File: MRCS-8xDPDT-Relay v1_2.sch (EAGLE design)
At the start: 36 parts, among them CON3 CONNECTOR-M10LOCK, CON5 CONNECTOR-M03MOLEX-254-LOCK, IC1 ULN2830, K1 G5V-2, K2 G5V-2, K3 G5V-2, K4 G5V-2, K5 G5V-2, K6 G5V-2, K7 G5V-2, K8 G5V-2

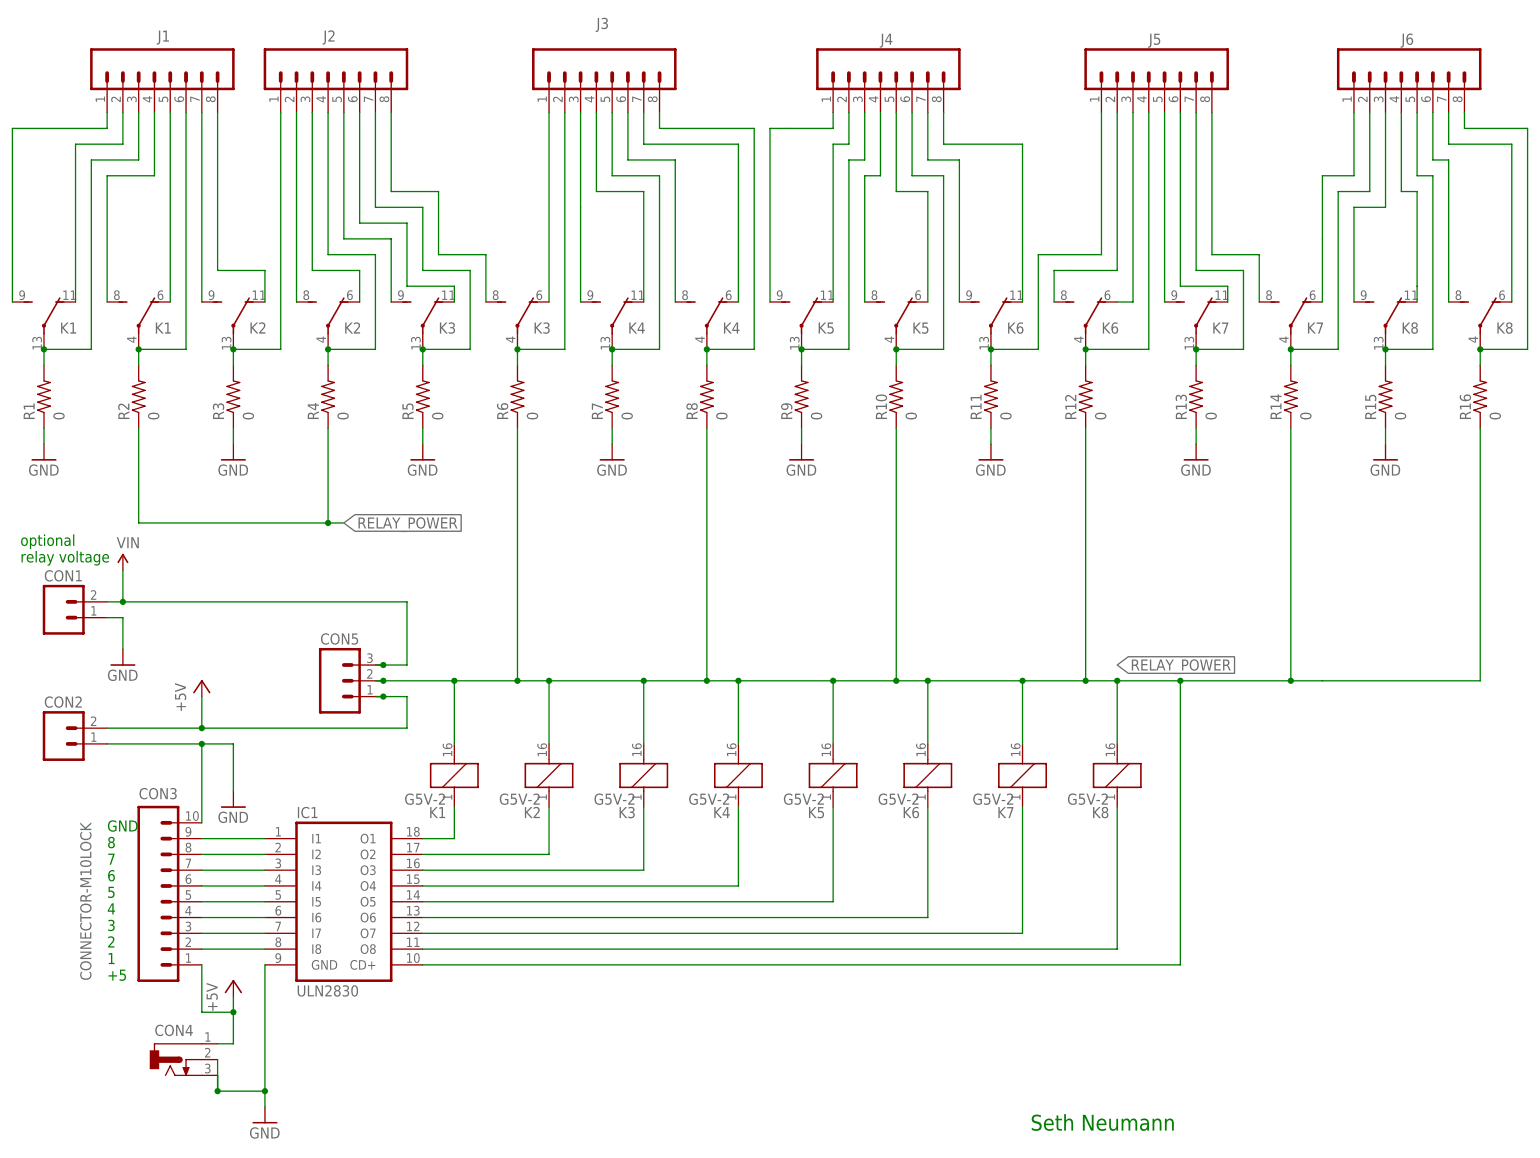
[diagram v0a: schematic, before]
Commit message: changes for V1.2
1 - changed polarity of relay so polarized relays will work
2 - Moved the second contact to a separate bus, so you can put any signal you want in by leaving the resistor uncut or cut it and use the contact independently
3 - added connector for bus above, cleaned up labels
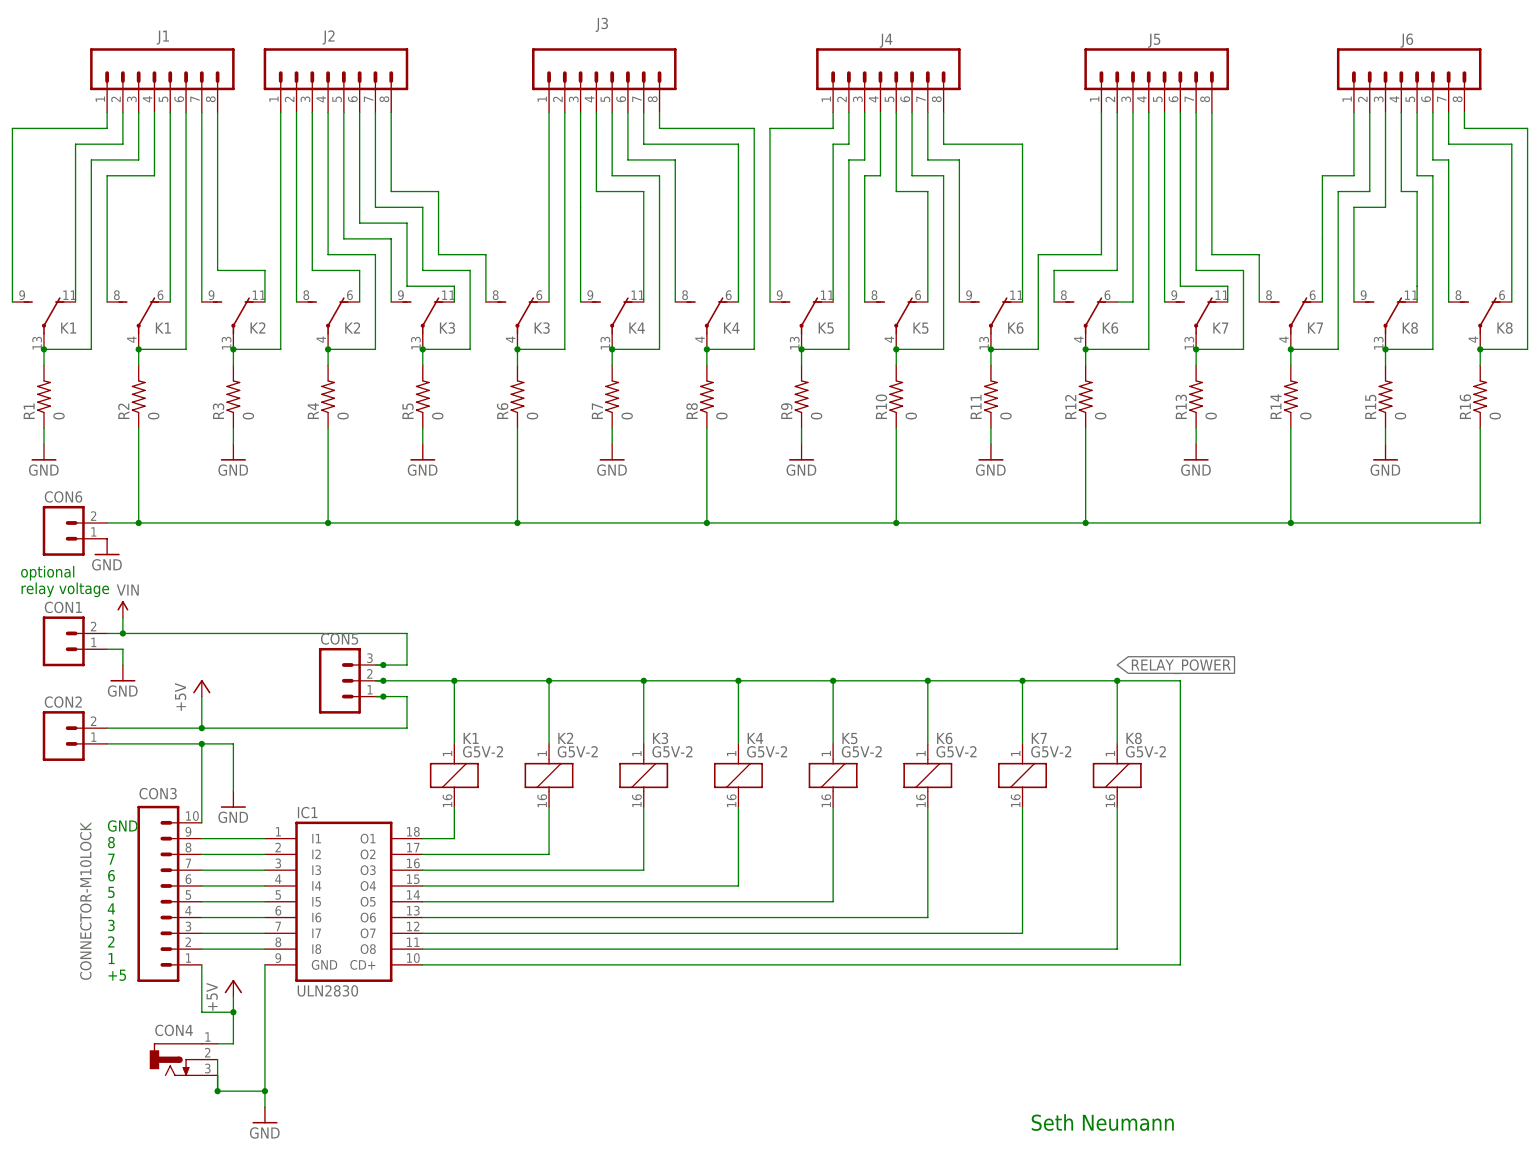
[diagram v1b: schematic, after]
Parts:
- added CON6: (no value), SPCoast:CONNECTOR-M023.5MM-LOCK
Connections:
- new net AUX_COMMON: CON6.B, R10.1, R12.1, R14.1, R16.1, R2.1, R4.1, R6.1, R8.1
- net GND: now also CON6.A
- net N$10: now also K3A.2; no longer K3A.1
- net N$11: now also K4A.2; no longer K4A.1
- net N$12: now also K5A.2; no longer K5A.1
- net N$14: now also K6A.2; no longer K6A.1
- net N$15: now also K7A.2; no longer K7A.1
- net N$16: now also K8A.2; no longer K8A.1
- net N$22: now also K1A.2; no longer K1A.1
- net N$9: now also K2A.2; no longer K2A.1
- net RELAY_POWER: now also K1A.1, K2A.1, K3A.1, K4A.1, K5A.1, K6A.1, K7A.1, K8A.1; no longer K1A.2, K2A.2, K3A.2, K4A.2, K5A.2, K6A.2, K7A.2, K8A.2, R10.1, R12.1, R14.1, R16.1, R2.1, R4.1, R6.1, R8.1
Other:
- moved on the sheet: CON1, K1, K2, K3, K4, K5, K6, K7, K8
